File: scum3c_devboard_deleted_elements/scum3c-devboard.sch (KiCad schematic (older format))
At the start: 6 parts, among them U9AB1 MPU-9250

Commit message: added placeholder battery
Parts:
- JA1: footprint (none) -> Connector_PinHeader_2.54mm:PinHeader_2x04_P2.54mm_Vertical
- JB1: footprint (none) -> Connector_PinHeader_2.54mm:PinHeader_2x05_P2.54mm_Vertical
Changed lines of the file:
@@
 F 0 "JA1" H 1950 5017 50  0000 C CNN
 F 1 "Conn_02x04_Odd_Even" H 1950 4926 50  0000 C CNN
-F 2 "" H 1900 4700 50  0001 C CNN
+F 2 "Connector_PinHeader_2.54mm:PinHeader_2x04_P2.54mm_Vertical" H 1900 4700 50  0001 C CNN
 F 3 "~" H 1900 4700 50  0001 C CNN
 	1    1900 4700
@@
 F 0 "JB1" H 4600 4917 50  0000 C CNN
 F 1 "Conn_02x05_Odd_Even" H 4600 4826 50  0000 C CNN
-F 2 "" H 4550 4500 50  0001 C CNN
+F 2 "Connector_PinHeader_2.54mm:PinHeader_2x05_P2.54mm_Vertical" H 4550 4500 50  0001 C CNN
 F 3 "~" H 4550 4500 50  0001 C CNN
 	1    4550 4500

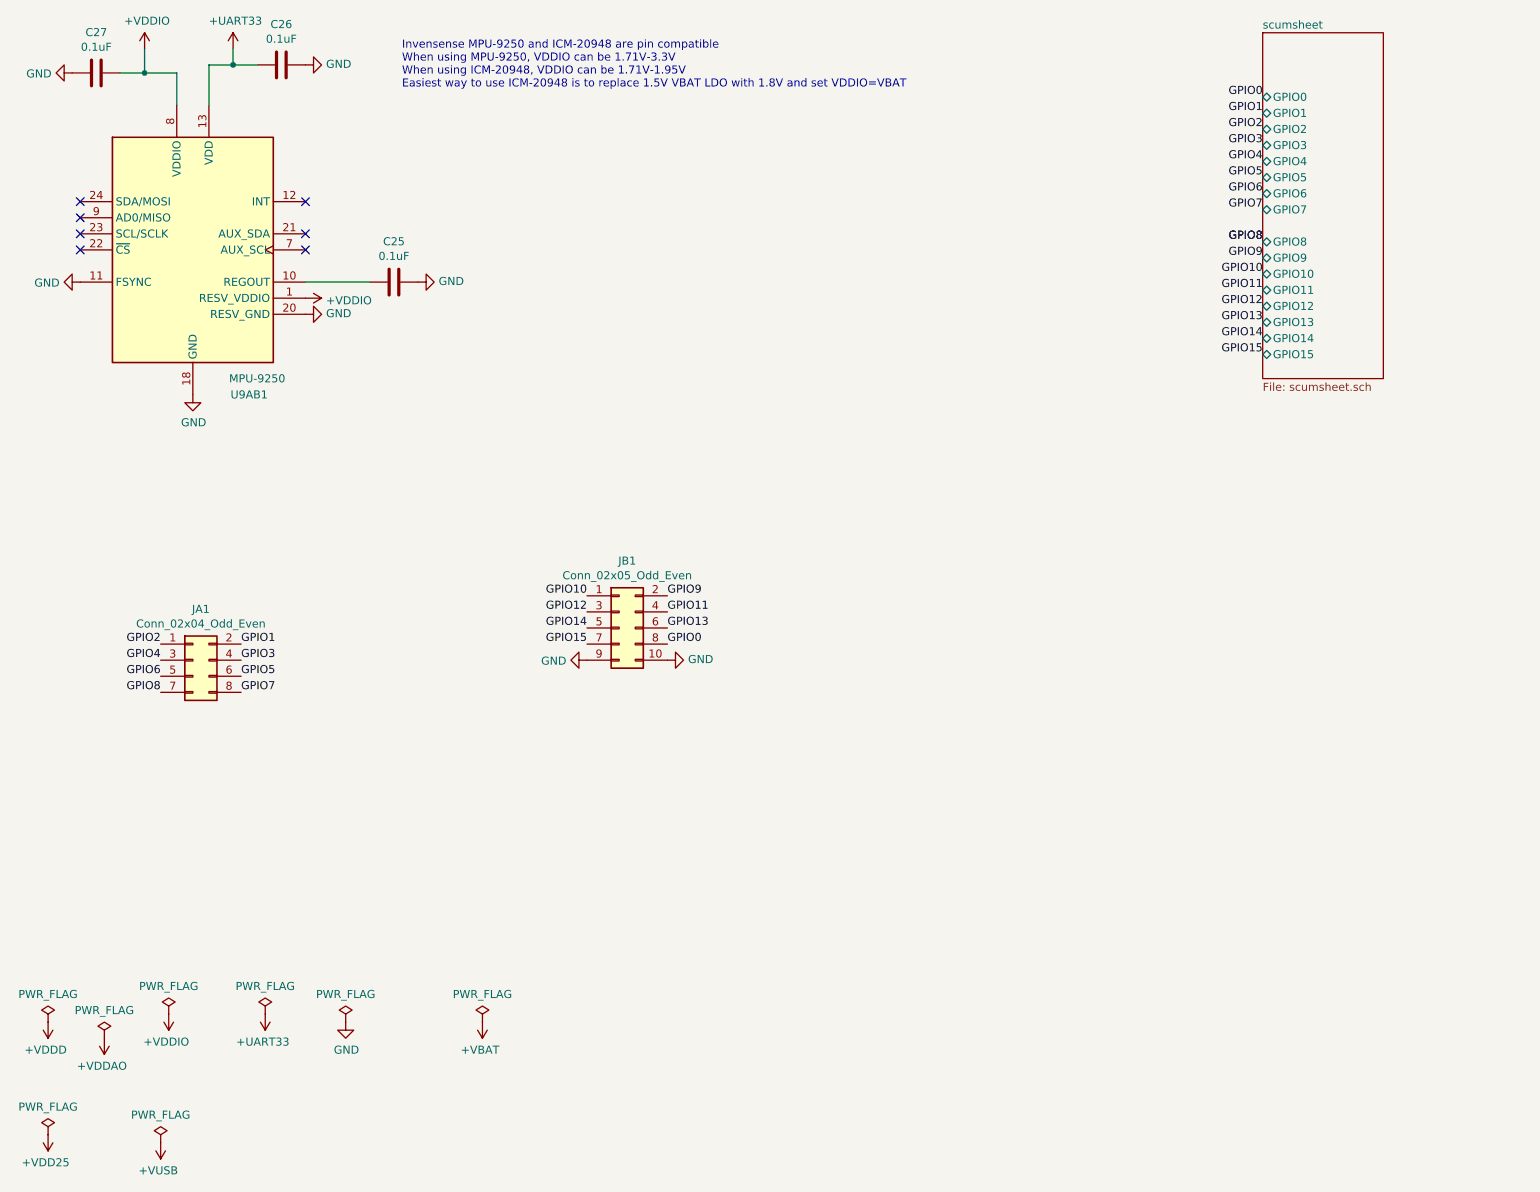
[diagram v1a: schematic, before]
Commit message: added zener diode voltage protection
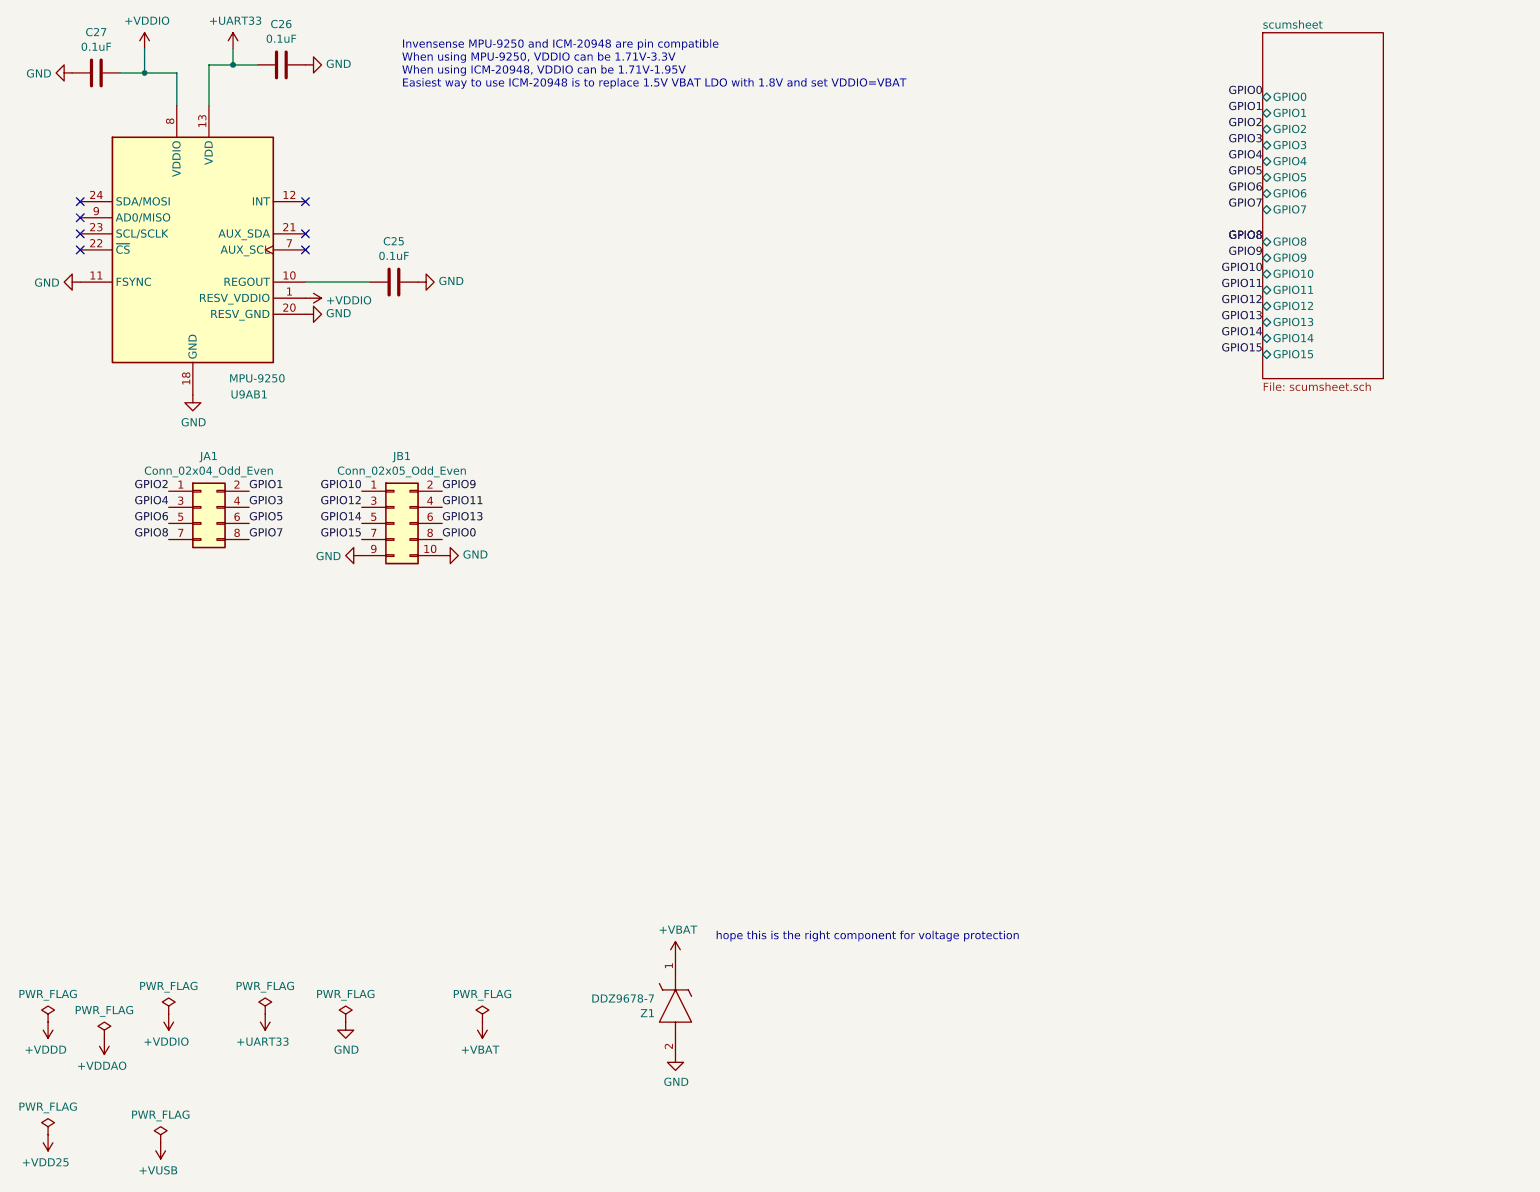
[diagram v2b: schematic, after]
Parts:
- added Z1: DDZ9678-7, SamacSys_Parts:SOD3716X135N, symbol SamacSys_Parts:DDZ9678-7
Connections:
- net +VBAT: now also Z1.1
- net GND: now also Z1.2
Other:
- note added: "hope this is the right component for voltage protection"
- moved on the sheet: JA1, JB1
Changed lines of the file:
@@
 	1    0    0    -1
 $EndComp
-Text Label 1700 4600 2    50   ~ 0
+Text Label 1750 3650 2    50   ~ 0
 GPIO2
-Text Label 2200 4600 0    50   ~ 0
+Text Label 2250 3650 0    50   ~ 0
 GPIO1
-Text Label 1700 4700 2    50   ~ 0
+Text Label 1750 3750 2    50   ~ 0
 GPIO4
-Text Label 1700 4800 2    50   ~ 0
+Text Label 1750 3850 2    50   ~ 0
 GPIO6
-Text Label 1700 4900 2    50   ~ 0
+Text Label 1750 3950 2    50   ~ 0
 GPIO8
-Text Label 2200 4900 0    50   ~ 0
+Text Label 2250 3950 0    50   ~ 0
 GPIO7
-Text Label 2200 4800 0    50   ~ 0
+Text Label 2250 3850 0    50   ~ 0
 GPIO5
-Text Label 2200 4700 0    50   ~ 0
+Text Label 2250 3750 0    50   ~ 0
 GPIO3
-Text Label 4350 4300 2    50   ~ 0
+Text Label 2950 3650 2    50   ~ 0
 GPIO10
-Text Label 4350 4400 2    50   ~ 0
+Text Label 2950 3750 2    50   ~ 0
 GPIO12
-Text Label 4350 4500 2    50   ~ 0
+Text Label 2950 3850 2    50   ~ 0
 GPIO14
-Text Label 4350 4600 2    50   ~ 0
+Text Label 2950 3950 2    50   ~ 0
 GPIO15
 $Comp
 L power:GND #PWR0111
 U 1 1 5F3EC8B2
-P 4350 4700
-F 0 "#PWR0111" H 4350 4450 50  0001 C CNN
-F 1 "GND" V 4355 4572 50  0000 R CNN
-F 2 "" H 4350 4700 50  0001 C CNN
-F 3 "" H 4350 4700 50  0001 C CNN
-	1    4350 4700
+P 2950 4050
+F 0 "#PWR0111" H 2950 3800 50  0001 C CNN
+F 1 "GND" V 2955 3922 50  0000 R CNN
+F 2 "" H 2950 4050 50  0001 C CNN
+F 3 "" H 2950 4050 50  0001 C CNN
+	1    2950 4050
 	0    1    1    0
 $EndComp
-Text Label 4850 4300 0    50   ~ 0
+Text Label 3450 3650 0    50   ~ 0
 GPIO9
-Text Label 4850 4600 0    50   ~ 0
+Text Label 3450 3950 0    50   ~ 0
 GPIO0
-Text Label 4850 4500 0    50   ~ 0
+Text Label 3450 3850 0    50   ~ 0
 GPIO13
-Text Label 4850 4400 0    50   ~ 0
+Text Label 3450 3750 0    50   ~ 0
 GPIO11
 $Comp
 L power:GND #PWR0112
 U 1 1 5F3ED1BB
-P 4850 4700
-F 0 "#PWR0112" H 4850 4450 50  0001 C CNN
-F 1 "GND" V 4855 4572 50  0000 R CNN
-F 2 "" H 4850 4700 50  0001 C CNN
-F 3 "" H 4850 4700 50  0001 C CNN
-	1    4850 4700
+P 3450 4050
+F 0 "#PWR0112" H 3450 3800 50  0001 C CNN
+F 1 "GND" V 3455 3922 50  0000 R CNN
+F 2 "" H 3450 4050 50  0001 C CNN
+F 3 "" H 3450 4050 50  0001 C CNN
+	1    3450 4050
 	0    -1   -1   0
 $EndComp
@@
 L Connector_Generic:Conn_02x04_Odd_Even JA1
 U 1 1 5F4FC0F5
-P 1900 4700
-F 0 "JA1" H 1950 5017 50  0000 C CNN
-F 1 "Conn_02x04_Odd_Even" H 1950 4926 50  0000 C CNN
-F 2 "Connector_PinHeader_2.54mm:PinHeader_2x04_P2.54mm_Vertical" H 1900 4700 50  0001 C CNN
-F 3 "~" H 1900 4700 50  0001 C CNN
-	1    1900 4700
+P 1950 3750
+F 0 "JA1" H 2000 4067 50  0000 C CNN
+F 1 "Conn_02x04_Odd_Even" H 2000 3976 50  0000 C CNN
+F 2 "Connector_PinHeader_2.54mm:PinHeader_2x04_P2.54mm_Vertical" H 1950 3750 50  0001 C CNN
+F 3 "~" H 1950 3750 50  0001 C CNN
+	1    1950 3750
 	1    0    0    -1
 $EndComp
@@
 L Connector_Generic:Conn_02x05_Odd_Even JB1
 U 1 1 5F4FD4BB
-P 4550 4500
-F 0 "JB1" H 4600 4917 50  0000 C CNN
-F 1 "Conn_02x05_Odd_Even" H 4600 4826 50  0000 C CNN
-F 2 "Connector_PinHeader_2.54mm:PinHeader_2x05_P2.54mm_Vertical" H 4550 4500 50  0001 C CNN
-F 3 "~" H 4550 4500 50  0001 C CNN
-	1    4550 4500
+P 3150 3850
+F 0 "JB1" H 3200 4267 50  0000 C CNN
+F 1 "Conn_02x05_Odd_Even" H 3200 4176 50  0000 C CNN
+F 2 "Connector_PinHeader_2.54mm:PinHeader_2x05_P2.54mm_Vertical" H 3150 3850 50  0001 C CNN
+F 3 "~" H 3150 3850 50  0001 C CNN
+	1    3150 3850
 	1    0    0    -1
 $EndComp
@@
 F17 "GPIO0" B L 8550 1200 50
 $EndSheet
+$Comp
+L SamacSys_Parts:DDZ9678-7 Z1
+U 1 1 5F7B30CA
+P 4900 6550
+F 0 "Z1" V 5246 6422 50  0000 R CNN
+F 1 "DDZ9678-7" V 5155 6422 50  0000 R CNN
+F 2 "SamacSys_Parts:SOD3716X135N" H 5300 6700 50  0001 L CNN
+F 3 "https://www.mouser.com/datasheet/2/115/ds30410-30695.pdf" H 5300 6600 50  0001 L CNN
+F 4 "Diode Zener 1.8V 5% 500mW 2Pin SOD123" H 5300 6500 50  0001 L CNN "Description"
+F 5 "1.35" H 5300 6400 50  0001 L CNN "Height"
+F 6 "Diodes Inc." H 5300 6300 50  0001 L CNN "Manufacturer_Name"
+F 7 "DDZ9678-7" H 5300 6200 50  0001 L CNN "Manufacturer_Part_Number"
+F 8 "DDZ9678-7" H 5300 6100 50  0001 L CNN "Arrow Part Number"
+F 9 "https://www.arrow.com/en/products/ddz9678-7/diodes-incorporated" H 5300 6000 50  0001 L CNN "Arrow Price/Stock"
+F 10 "621-DDZ9678-7" H 5300 5900 50  0001 L CNN "Mouser Part Number"
+F 11 "https://www.mouser.co.uk/ProductDetail/Diodes-Incorporated/DDZ9678-7?qs=ptj1V1atRAp2rXEOTrnLaA%3D%3D" H 5300 5800 50  0001 L CNN "Mouser Price/Stock"
+	1    4900 6550
+	0    1    1    0
+$EndComp
+$Comp
+L power:GND #PWR0122
+U 1 1 5F7B8192
+P 4900 7150
+F 0 "#PWR0122" H 4900 6900 50  0001 C CNN
+F 1 "GND" H 4905 6977 50  0000 C CNN
+F 2 "" H 4900 7150 50  0001 C CNN
+F 3 "" H 4900 7150 50  0001 C CNN
+	1    4900 7150
+	1    0    0    -1
+$EndComp
+$Comp
+L draft1library:+VBAT #PWR0123
+U 1 1 5F7BC62D
+P 4900 6550
+F 0 "#PWR0123" H 4900 6400 50  0001 C CNN
+F 1 "+VBAT" H 4915 6723 50  0000 C CNN
+F 2 "" H 4900 6550 50  0001 C CNN
+F 3 "" H 4900 6550 50  0001 C CNN
+	1    4900 6550
+	1    0    0    -1
+$EndComp
+Text Notes 5150 6450 0    50   ~ 0
+hope this is the right component for voltage protection
 $EndSCHEMATC
